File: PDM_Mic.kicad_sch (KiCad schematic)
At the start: 33 parts, among them J10 JST_SH_1x4_BM04B-SRSS-TB-LF-SN, J4 Conn_FFC_Molex_5019510550, J5 Conn_FFC_Molex_5019510550, U18 TPD4E05U06QDQARQ1, U19 TPD4E05U06QDQARQ1, U20 TLV73318PDBVT, U21 ADAU7118ACPZRL

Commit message: [#75544] Add license and logotype
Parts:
- R89, R96: now left out of the parts list

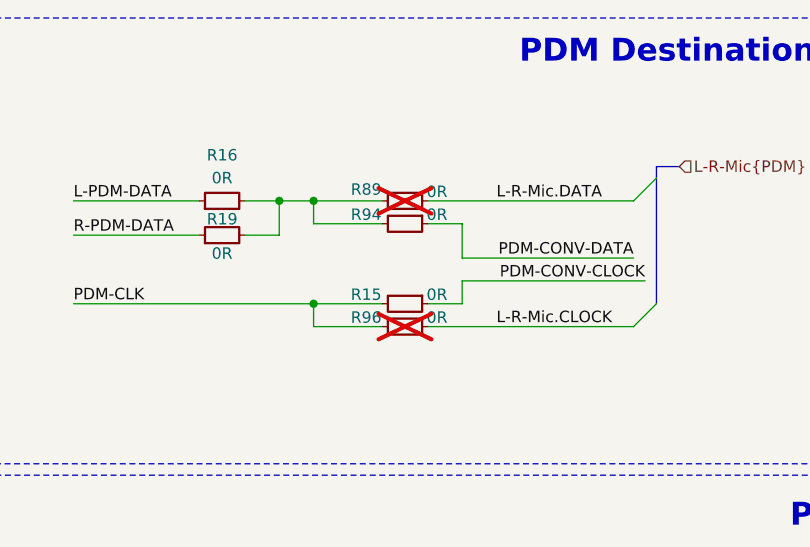
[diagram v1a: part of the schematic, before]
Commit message: [#75930] Change DNP configuration to PDM
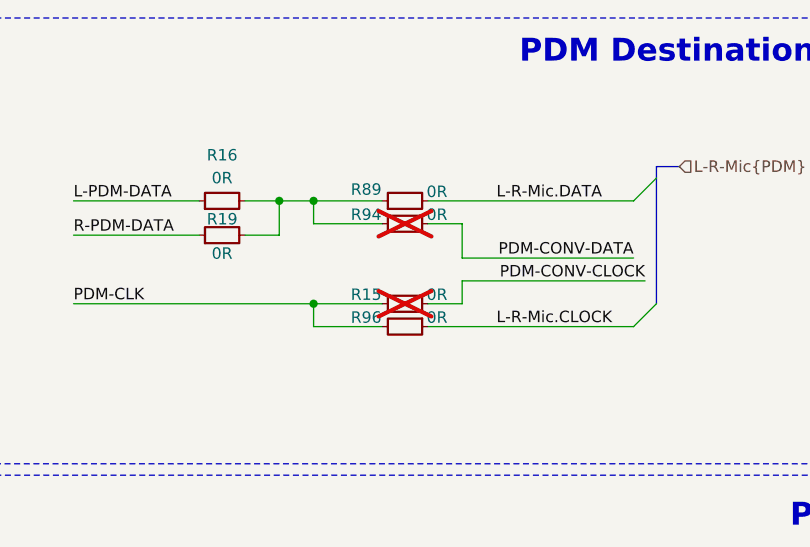
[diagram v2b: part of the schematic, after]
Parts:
- R15, R94: now not fitted; now left out of the parts list
- R89, R96: now fitted; now in the parts list

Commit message: [#77779] Rename to audio latency tester board
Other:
- title: Audio controller board -> Audio latency tester board
